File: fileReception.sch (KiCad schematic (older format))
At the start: 20 parts, among them U10 74AHC1G08, U11 74AHC1G32, U12 74AHC1G04, U13 74AHC595, U6 LTC6994xS6-1, U7 LTC6990CS6, U8 CD74AC161M, U9 74HCT107

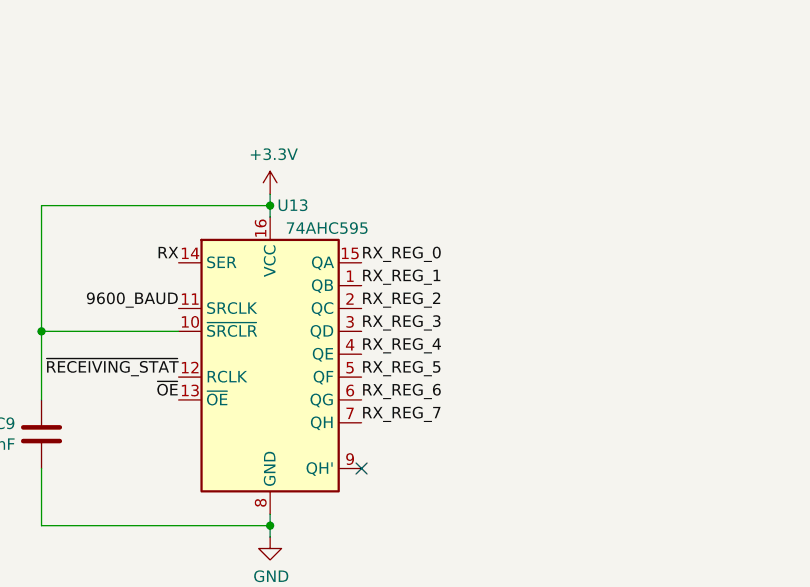
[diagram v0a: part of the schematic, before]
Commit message: Fixing LSB first issue #1
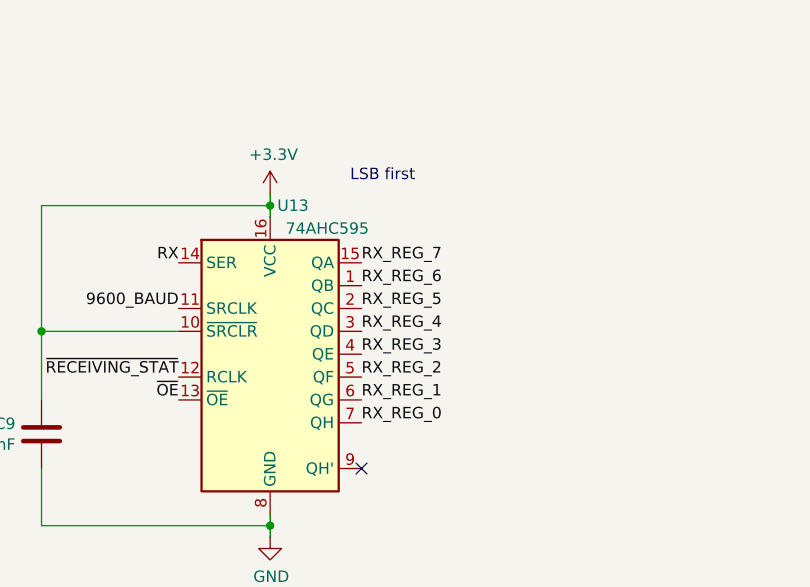
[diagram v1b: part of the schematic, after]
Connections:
- net RX_REG_0: now also U13.7 (QH); no longer U13.15 (QA)
- net RX_REG_1: now also U13.6 (QG); no longer U13.1 (QB)
- net RX_REG_2: now also U13.5 (QF); no longer U13.2 (QC)
- net RX_REG_3: now also U13.4 (QE); no longer U13.3 (QD)
- net RX_REG_4: now also U13.3 (QD); no longer U13.4 (QE)
- net RX_REG_5: now also U13.2 (QC); no longer U13.5 (QF)
- net RX_REG_6: now also U13.1 (QB); no longer U13.6 (QG)
- net RX_REG_7: now also U13.15 (QA); no longer U13.7 (QH)
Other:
- note added: "LSB first"
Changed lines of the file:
@@
 Wire Wire Line
 	6850 2300 7000 2300
+Text Label 9200 4850 0    50   ~ 0
+RX_REG_0
+Text Label 9200 4750 0    50   ~ 0
+RX_REG_1
+Text Label 9200 4650 0    50   ~ 0
+RX_REG_2
+Text Label 9200 4550 0    50   ~ 0
+RX_REG_3
+Text Label 9200 4450 0    50   ~ 0
+RX_REG_4
+Text Label 9200 4350 0    50   ~ 0
+RX_REG_5
+Text Label 9200 4250 0    50   ~ 0
+RX_REG_6
 Text Label 9200 4150 0    50   ~ 0
-RX_REG_0
-Text Label 9200 4250 0    50   ~ 0
-RX_REG_1
-Text Label 9200 4350 0    50   ~ 0
-RX_REG_2
-Text Label 9200 4450 0    50   ~ 0
-RX_REG_3
-Text Label 9200 4550 0    50   ~ 0
-RX_REG_4
-Text Label 9200 4650 0    50   ~ 0
-RX_REG_5
-Text Label 9200 4750 0    50   ~ 0
-RX_REG_6
-Text Label 9200 4850 0    50   ~ 0
 RX_REG_7
 Text Label 10400 750  2    50   ~ 0
@@
 Wire Wire Line
 	3300 4850 2800 4850
+Text Notes 9150 3800 0    50   ~ 0
+LSB first
 $EndSCHEMATC

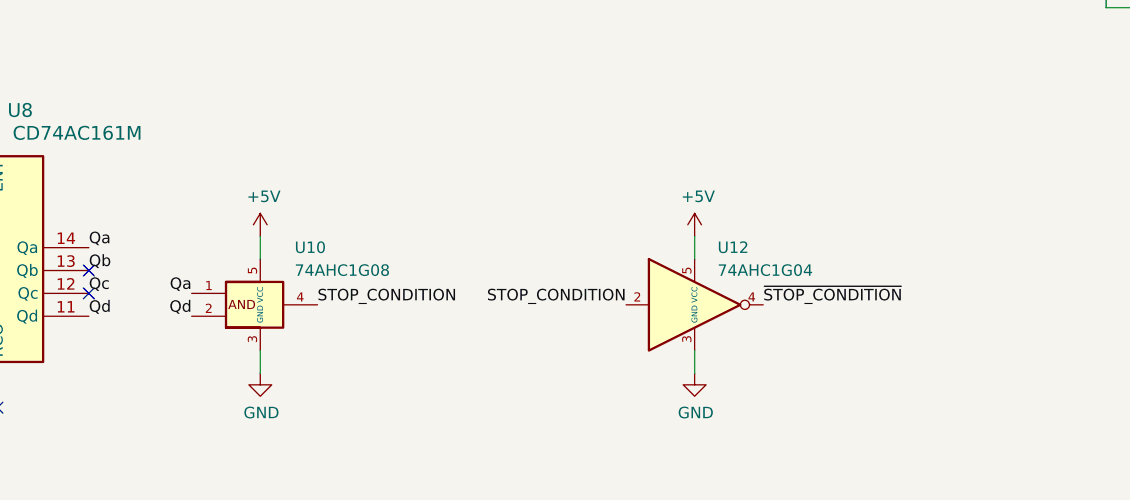
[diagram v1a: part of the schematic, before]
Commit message: Optimize gates count by replacing AND,INV with NAND
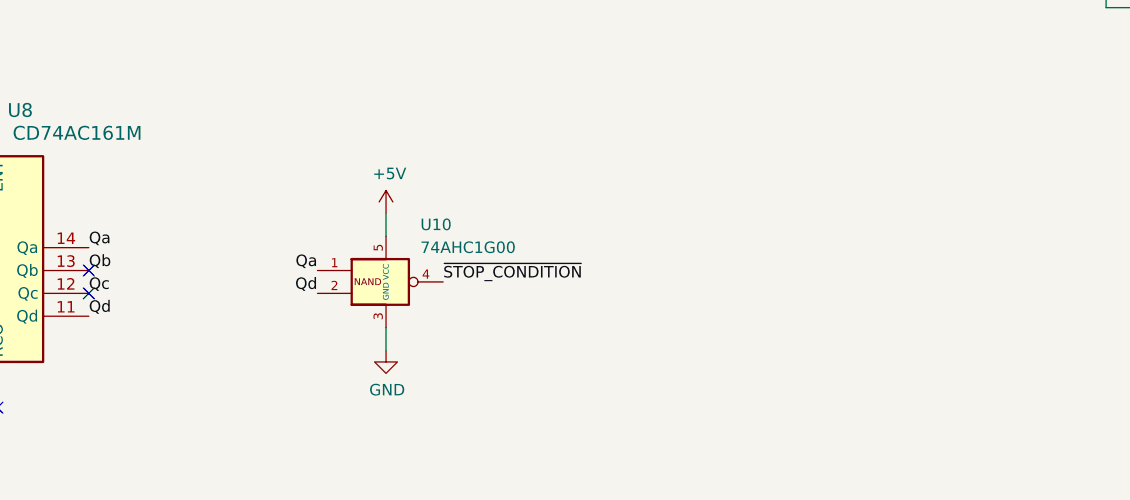
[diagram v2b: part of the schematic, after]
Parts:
- removed U10: 74AHC1G08, Package_TO_SOT_SMD:SOT-23-5, symbol Custom:74AHC1G08
- removed U12: 74AHC1G04, Package_TO_SOT_SMD:SOT-23-5, symbol Custom:74AHC1G04
- added U10: 74AHC1G00, symbol Custom:74AHC1G00
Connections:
- net +5V: now also U10.5 (VCC)
- net GND: now also U10.3 (GND)
- net Qa: now also U10.1
- net Qd: now also U10.2
- net ~STOP_CONDITION: now also U10.4
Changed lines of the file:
@@
 	1    0    0    -1
 $EndComp
-$Comp
-L Custom:74AHC1G04 U12
-U 1 1 5FD80E5A
-P 6000 6600
-F 0 "U12" H 6100 6850 50  0000 L CNN
-F 1 "74AHC1G04" H 6100 6750 50  0000 L CNN
-F 2 "Package_TO_SOT_SMD:SOT-23-5" H 6000 6600 50  0001 C CNN
-F 3 "https://assets.nexperia.com/documents/data-sheet/74AHC_AHCT1G04.pdf" H 6000 6600 50  0001 C CNN
-	1    6000 6600
-	1    0    0    -1
-$EndComp
-Text Label 4350 6600 0    50   ~ 0
-STOP_CONDITION
 Text Label 5050 4250 2    50   ~ 0
 9600_BAUD
@@
 $EndComp
 $Comp
-L power:+5V #PWR037
-U 1 1 5FD9F95B
-P 6000 6300
-F 0 "#PWR037" H 6000 6150 50  0001 C CNN
-F 1 "+5V" H 6015 6473 50  0000 C CNN
-F 2 "" H 6000 6300 50  0001 C CNN
-F 3 "" H 6000 6300 50  0001 C CNN
-	1    6000 6300
-	1    0    0    -1
-$EndComp
-$Comp
 L power:GND #PWR028
 U 1 1 5FDA094E
@@
 	1    0    0    -1
 $EndComp
-$Comp
-L power:GND #PWR038
-U 1 1 5FDA197E
-P 6000 6900
-F 0 "#PWR038" H 6000 6650 50  0001 C CNN
-F 1 "GND" H 6005 6727 50  0000 C CNN
-F 2 "" H 6000 6900 50  0001 C CNN
-F 3 "" H 6000 6900 50  0001 C CNN
-	1    6000 6900
-	1    0    0    -1
-$EndComp
-Wire Wire Line
-	6000 6800 6000 6900
-Wire Wire Line
-	6000 6400 6000 6300
 Wire Wire Line
 	2850 7150 2850 7100
@@
 	8800 5300 8800 5250
 $Comp
-L Custom:74AHC1G08 U?
-U 1 1 5FDAE04C
-P 4100 6600
-AR Path="/5FE44E7A/5FDAE04C" Ref="U?"  Part="1"
-AR Path="/5FD66C52/5FDAE04C" Ref="U10"  Part="1"
-F 0 "U10" H 4250 6850 50  0000 L CNN
-F 1 "74AHC1G08" H 4250 6750 50  0000 L CNN
-F 2 "Package_TO_SOT_SMD:SOT-23-5" H 4100 6600 50  0001 C CNN
-F 3 "https://assets.nexperia.com/documents/data-sheet/74AHC_AHCT1G08.pdf" H 4100 6600 50  0001 C CNN
-	1    4100 6600
-	1    0    0    -1
-$EndComp
-$Comp
 L power:GND #PWR?
 U 1 1 5FDAE052
-P 4100 6900
+P 4650 6800
 AR Path="/5FE44E7A/5FDAE052" Ref="#PWR?"  Part="1"
 AR Path="/5FD66C52/5FDAE052" Ref="#PWR032"  Part="1"
-F 0 "#PWR032" H 4100 6650 50  0001 C CNN
-F 1 "GND" H 4105 6727 50  0000 C CNN
-F 2 "" H 4100 6900 50  0001 C CNN
-F 3 "" H 4100 6900 50  0001 C CNN
-	1    4100 6900
+F 0 "#PWR032" H 4650 6550 50  0001 C CNN
+F 1 "GND" H 4655 6627 50  0000 C CNN
+F 2 "" H 4650 6800 50  0001 C CNN
+F 3 "" H 4650 6800 50  0001 C CNN
+	1    4650 6800
 	1    0    0    -1
 $EndComp
@@
 L power:+5V #PWR?
 U 1 1 5FDAE058
-P 4100 6300
+P 4650 6200
 AR Path="/5FE44E7A/5FDAE058" Ref="#PWR?"  Part="1"
 AR Path="/5FD66C52/5FDAE058" Ref="#PWR031"  Part="1"
-F 0 "#PWR031" H 4100 6150 50  0001 C CNN
-F 1 "+5V" H 4115 6473 50  0000 C CNN
-F 2 "" H 4100 6300 50  0001 C CNN
-F 3 "" H 4100 6300 50  0001 C CNN
-	1    4100 6300
-	1    0    0    -1
-$EndComp
-Wire Wire Line
-	4100 6400 4100 6300
-Wire Wire Line
-	4100 6800 4100 6900
+F 0 "#PWR031" H 4650 6050 50  0001 C CNN
+F 1 "+5V" H 4665 6373 50  0000 C CNN
+F 2 "" H 4650 6200 50  0001 C CNN
+F 3 "" H 4650 6200 50  0001 C CNN
+	1    4650 6200
+	1    0    0    -1
+$EndComp
+Wire Wire Line
+	4650 6300 4650 6200
+Wire Wire Line
+	4650 6700 4650 6800
 Text Label 3350 6350 0    50   ~ 0
 Qa
@@
 NoConn ~ 3350 6450
 NoConn ~ 3350 6550
-Text Label 3800 6550 2    50   ~ 0
+Text Label 4350 6450 2    50   ~ 0
 Qa
-Text Label 3800 6650 2    50   ~ 0
+Text Label 4350 6550 2    50   ~ 0
 Qd
-Text Label 5700 6600 2    50   ~ 0
-STOP_CONDITION
-Text Label 6300 6600 0    50   ~ 0
+Text Label 4900 6500 0    50   ~ 0
 ~STOP_CONDITION
 Text Label 5050 4350 2    50   ~ 0
@@
 Text Notes 9150 3800 0    50   ~ 0
 LSB first
+$Comp
+L Custom:74AHC1G00 U?
+U 1 1 609D75AB
+P 4650 6500
+AR Path="/609D75AB" Ref="U?"  Part="1"
+AR Path="/5FD66C52/609D75AB" Ref="U10"  Part="1"
+F 0 "U10" H 4800 6750 50  0000 L CNN
+F 1 "74AHC1G00" H 4800 6650 50  0000 L CNN
+F 2 "" H 4650 6500 50  0001 C CNN
+F 3 "https://assets.nexperia.com/documents/data-sheet/74AHC_AHCT1G00.pdf" H 4650 6500 50  0001 C CNN
+	1    4650 6500
+	1    0    0    -1
+$EndComp
 $EndSCHEMATC
